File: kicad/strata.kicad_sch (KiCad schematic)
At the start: 80 parts, among them J1 Eurorack Mono Jack, J10 Conn_01x02_Male, J11 Conn_01x04_Male, J12 Conn_01x04_Female, J13 Conn_01x08_Male, J14 Eurorack Mono Jack, J15 Conn_01x08_Female, J16 Eurorack Mono Jack, J17 Eurorack Mono Jack, J18 Eurorack Mono Jack, J19 Eurorack Mono Jack, J2 Eurorack Mono Jack, J20 Eurorack Mono Jack, J24 Eurorack Mono Jack, J25 Eurorack Mono Jack, J26 Eurorack Mono Jack, J27 Eurorack Mono Jack, J28 Eurorack Mono Jack, J29 Eurorack Mono Jack, J3 Eurorack Mono Jack, J30 Eurorack Mono Jack, J31 Eurorack Mono Jack, J32 Conn_01x08_Female, J33 Eurorack Mono Jack, J34 Conn_01x08_Male, J35 Conn_01x08_Female, J36 Conn_01x08_Male, J37 Eurorack Power Small, J38 Conn_02x04_Odd_Even, J4 Eurorack Mono Jack, J49 Eurorack Mono Jack, J5 Conn_01x04_Female, J50 Eurorack Mono Jack, J51 Eurorack Mono Jack, J52 Conn_01x04_Female, J53 Conn_01x04_Male, J6 Conn_01x06_Female, J7 Conn_01x04_Male, J8 Conn_01x06_Male, J9 Conn_01x02_Female, U1 TL072, U2 L78L05_TO92

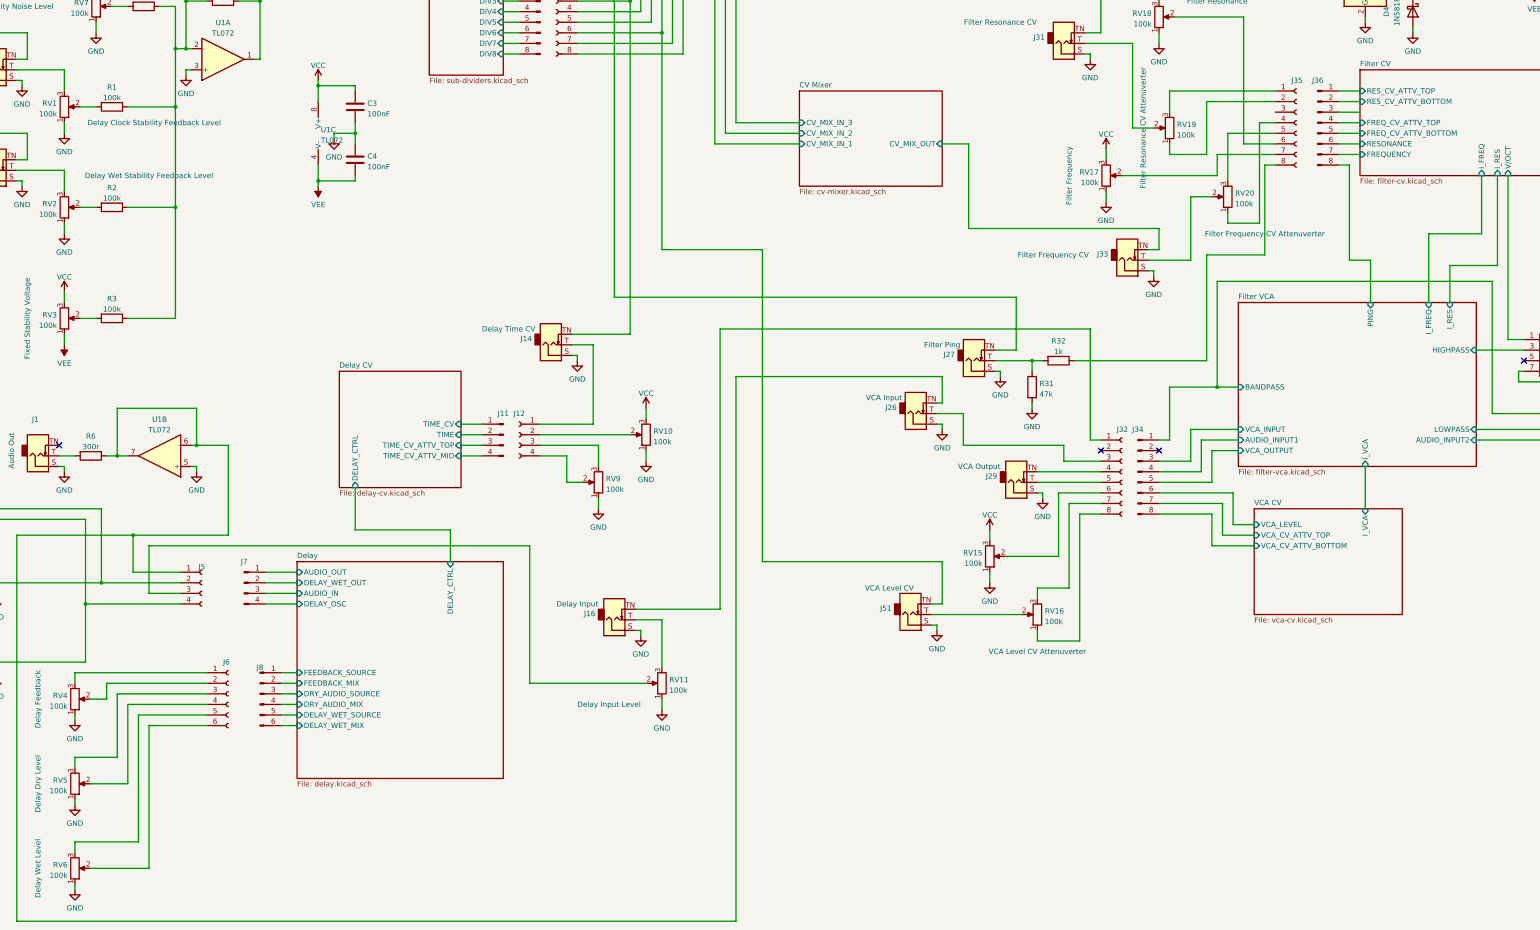
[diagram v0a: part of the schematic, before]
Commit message: component positioning mostly done
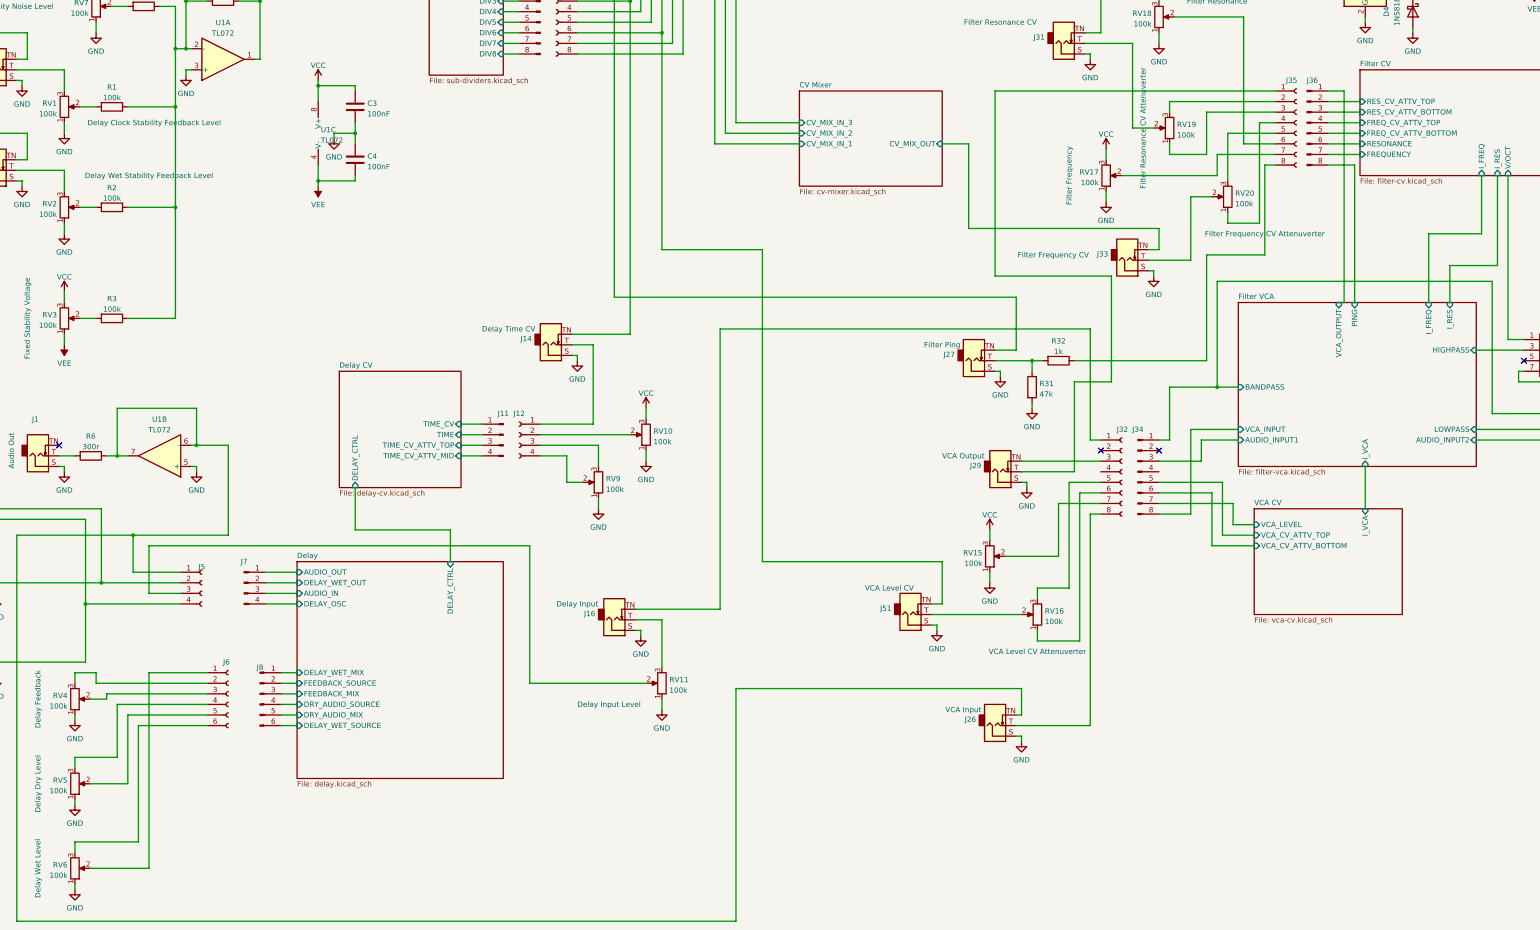
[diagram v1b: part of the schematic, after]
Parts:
- C1, C3, C4: footprint rumblesan-standard-parts:C_Rect_L7.0mm_W3.5mm_P5.00mm -> rumblesan-standard-parts:C_Rect_L7.0mm_W2.5mm_P5.00mm
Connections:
- net Delay/DELAY_WET_MIX: now also J8.1 (Pin_1); no longer J8.6 (Pin_6)
- net Delay/DELAY_WET_SOURCE: now also J8.6 (Pin_6); no longer J8.5 (Pin_5)
- net Delay/DRY_AUDIO_MIX: now also J8.5 (Pin_5); no longer J8.4 (Pin_4)
- net Delay/DRY_AUDIO_SOURCE: now also J8.4 (Pin_4); no longer J8.3 (Pin_3)
- net Delay/FEEDBACK_MIX: now also J8.3 (Pin_3); no longer J8.2 (Pin_2)
- net Delay/FEEDBACK_SOURCE: now also J8.2 (Pin_2); no longer J8.1 (Pin_1)
- net Filter CV/RES_CV_ATTV_BOTTOM: now also J36.3 (Pin_3); no longer J36.2 (Pin_2)
- net Filter CV/RES_CV_ATTV_TOP: now also J36.2 (Pin_2); no longer J36.1 (Pin_1)
- net Filter VCA/AUDIO_INPUT1: now also J34.3 (Pin_3); no longer J34.4 (Pin_4)
- net Filter VCA/VCA_INPUT: now also J34.8 (Pin_8); no longer J34.3 (Pin_3)
- net Filter VCA/VCA_OUTPUT: now also J36.1 (Pin_1); no longer J34.5 (Pin_5)
- net VCA CV/VCA_CV_ATTV_BOTTOM: now also J34.6 (Pin_6); no longer J34.8 (Pin_8)
- net VCA CV/VCA_CV_ATTV_TOP: now also J34.5 (Pin_5); no longer J34.7 (Pin_7)
- net VCA CV/VCA_LEVEL: now also J34.7 (Pin_7); no longer J34.6 (Pin_6)
- net at RV4.2: now also J6.3 (Pin_3); no longer J6.2 (Pin_2)
- net at RV4.3: now also J6.2 (Pin_2); no longer J6.1 (Pin_1)
- net at J35.1 (Pin_1): now also J29.T (Tip); no longer RV19.3
- net at J35.2 (Pin_2): now also RV19.3; no longer RV19.1
- net at J35.3 (Pin_3): now also RV19.1
- net at RV5.2: now also J6.5 (Pin_5); no longer J6.4 (Pin_4)
- net at RV5.3: now also J6.4 (Pin_4); no longer J6.3 (Pin_3)
- net at RV6.3: now also J6.6 (Pin_6); no longer J6.5 (Pin_5)
- net at RV6.2: now also J6.1 (Pin_1); no longer J6.6 (Pin_6)
- net at J32.3 (Pin_3): now also J29.TN (Tip_normalize); no longer J26.T (Tip)
- net at J32.4 (Pin_4): no longer J29.TN (Tip_normalize)
- net at J32.5 (Pin_5): now also RV16.3; no longer J29.T (Tip)
- net at J32.6 (Pin_6): now also RV16.1; no longer RV15.2
- net at J32.7 (Pin_7): now also RV15.2; no longer RV16.3
- net at J32.8 (Pin_8): now also J26.T (Tip); no longer RV16.1
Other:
- moved on the sheet: J26, J29, J36

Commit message: initial layout done
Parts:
- removed H2, H4: MountingHole_Pad, rumblesan-standard-parts:MountingHole_3.2mm_M3_DIN965_Pad, symbol Mechanical:MountingHole_Pad
- removed J32: Conn_01x08_Female, Connector_PinSocket_2.54mm:PinSocket_1x08_P2.54mm_Vertical, symbol Connector:Conn_01x08_Female
- removed J34: Conn_01x08_Male, Connector_PinHeader_2.54mm:PinHeader_1x08_P2.54mm_Vertical, symbol Connector:Conn_01x08_Male
- added J32: Conn_01x06_Female, Connector_PinSocket_2.54mm:PinSocket_1x06_P2.54mm_Vertical, symbol Connector:Conn_01x06_Female
- added J34: Conn_01x06_Male, Connector_PinHeader_2.54mm:PinHeader_1x06_P2.54mm_Vertical, symbol Connector:Conn_01x06_Male
- added R157: 100k, rumblesan-standard-parts:R_Axial_DIN0207_L6.3mm_D2.5mm_P10.16mm_Horizontal, symbol rumblesan-standard-parts:R
- added R65: 47k, rumblesan-standard-parts:R_Axial_DIN0207_L6.3mm_D2.5mm_P10.16mm_Horizontal, symbol rumblesan-standard-parts:R
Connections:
- net CV Mixer/CV_MIX_IN_1: now also J15.4 (Pin_4); no longer J15.3 (Pin_3)
- net Filter CV/FREQ_CV_ATTV_BOTTOM: now also J36.4 (Pin_4); no longer J36.5 (Pin_5)
- net Filter CV/FREQ_CV_ATTV_TOP: now also J36.3 (Pin_3); no longer J36.4 (Pin_4)
- net Filter CV/RES_CV_ATTV_BOTTOM: now also J36.5 (Pin_5); no longer J36.3 (Pin_3)
- net Filter CV/V/OCT: now also J38.3 (Pin_3); no longer J38.1 (Pin_1)
- net Filter VCA/AUDIO_INPUT1: now also J34.5 (Pin_5)
- net Filter VCA/BANDPASS: now also J34.6 (Pin_6)
- net Filter VCA/HIGHPASS: now also J38.1 (Pin_1); no longer J38.3 (Pin_3)
- net Filter VCA/VCA_INPUT: now also J34.2 (Pin_2)
- net GND: now also R157.2, R65.1; no longer U1.5 (+)
- net Sub Dividers/DIV3: now also J13.4 (Pin_4); no longer J13.3 (Pin_3)
- net Sub Dividers/DIV4: now also J13.3 (Pin_3); no longer J13.4 (Pin_4)
- net VCA CV/VCA_CV_ATTV_BOTTOM: now also J34.3 (Pin_3)
- net VCA CV/VCA_CV_ATTV_TOP: now also J34.1 (Pin_1)
- net VCA CV/VCA_LEVEL: now also J34.4 (Pin_4)
- net at C1.2, J9.2 (Pin_2), R5.1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: now also R65.2
- net at R6.1, U1.6 (-), U1.7: no longer J26.TN (Tip_normalize), J5.1 (Pin_1)
- net at J16.TN (Tip_normalize): now also J32.6 (Pin_6)
- net at J35.3 (Pin_3): now also RV20.3; no longer RV19.1
- net at J35.5 (Pin_5): now also RV19.1; no longer RV20.3
- net at J20.T (Tip), J31.TN (Tip_normalize): now also J15.3 (Pin_3); no longer J15.4 (Pin_4)
- net at J29.TN (Tip_normalize): now also J32.5 (Pin_5)
- net at RV16.3: now also J32.1 (Pin_1)
- net at RV16.1: now also J32.3 (Pin_3)
- net at RV15.2: now also J32.4 (Pin_4)
- net at J26.T (Tip): now also J32.2 (Pin_2)
- new net: J26.TN (Tip_normalize), J5.1 (Pin_1), R157.1, U1.5 (+)
- no-connect marks 15 -> 13
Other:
- removed sheet Filter Expander
- moved on the sheet: J1, J26, J27, J29, J51, J6, J8, R31, R32, R6, RV15, RV16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

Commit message: Final changes for rev01
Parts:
- added C72: 22pF, rumblesan-standard-parts:C_Rect_L7.0mm_W2.5mm_P5.00mm, symbol rumblesan-standard-parts:C
- added C73: 1uF, rumblesan-standard-parts:CP_Radial_D5.0mm_P2.00mm, symbol rumblesan-standard-parts:C_Polarized
- added J39: Conn_01x03_Male, Connector_PinHeader_2.54mm:PinHeader_1x03_P2.54mm_Vertical, symbol Connector:Conn_01x03_Male
- added Q17: 2N3904, Package_TO_SOT_THT:TO-92_Inline_Wide, symbol Transistor_BJT:2N3904
- added R158, R159, R160: 10k, rumblesan-standard-parts:R_Axial_DIN0207_L6.3mm_D2.5mm_P10.16mm_Horizontal, symbol rumblesan-standard-parts:R
- added R161: 47k, rumblesan-standard-parts:R_Axial_DIN0207_L6.3mm_D2.5mm_P10.16mm_Horizontal, symbol rumblesan-standard-parts:R
- added R162: 47k, rumblesan-standard-parts:R_Axial_DIN0207_L6.3mm_D2.5mm_P2.54mm_Vertical, symbol rumblesan-standard-parts:R
- added R163, R166, R167, R168, R170, R171: 330r, rumblesan-standard-parts:R_Axial_DIN0207_L6.3mm_D2.5mm_P10.16mm_Horizontal, symbol rumblesan-standard-parts:R
- added R164, R165, R169, R172, R173: 330r, rumblesan-standard-parts:R_Axial_DIN0207_L6.3mm_D2.5mm_P2.54mm_Vertical, symbol rumblesan-standard-parts:R
- R6: value 300r -> 100k
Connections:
- net CV Mixer/CV_MIX_IN_1: now also R167.2; no longer J19.T (Tip)
- net CV Mixer/CV_MIX_IN_2: now also R169.2; no longer J24.T (Tip)
- net CV Mixer/CV_MIX_IN_3: now also R172.2; no longer J28.T (Tip)
- net Delay/DELAY_WET_SOURCE: now also J8.2 (Pin_2); no longer J8.6 (Pin_6)
- net Delay/DRY_AUDIO_MIX: now also J8.3 (Pin_3); no longer J8.5 (Pin_5)
- net Delay/DRY_AUDIO_SOURCE: now also J8.5 (Pin_5); no longer J8.4 (Pin_4)
- net Delay/FEEDBACK_MIX: now also J8.6 (Pin_6); no longer J8.3 (Pin_3)
- net Delay/FEEDBACK_SOURCE: now also J8.4 (Pin_4); no longer J8.2 (Pin_2)
- net GND: now also U1.5 (+), R162.1; no longer R157.2
- net Noise/NOISE: now also R165.1; no longer J4.T (Tip)
- net VCC: now also Q17.3 (C), R158.1; no longer RV3.3
- net VEE: now also R159.2, R160.1; no longer RV3.1
- net at J9.2 (Pin_2), R65.2, U1.1: now also R157.2, C72.2; no longer C1.2, R5.1
- net at C1.1, R1.1, R2.1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: now also U1.6 (-); no longer U1.2 (-)
- net at RV4.2: now also J6.6 (Pin_6); no longer J6.3 (Pin_3)
- net at RV4.3: now also J6.4 (Pin_4); no longer J6.2 (Pin_2)
- net at J3.TN (Tip_normalize), J5.2 (Pin_2): now also R164.2; no longer J49.T (Tip)
- net at J2.TN (Tip_normalize), J5.4 (Pin_4): now also R163.2; no longer J50.T (Tip)
- net at R6.1, U1.7: now also C1.2, R5.1; no longer U1.6 (-)
- net at J15.3 (Pin_3), J31.TN (Tip_normalize): now also R168.2; no longer J20.T (Tip)
- net at J30.T (Tip): now also R173.1; no longer J15.8 (Pin_8)
- net at RV5.2: now also J6.3 (Pin_3); no longer J6.5 (Pin_5)
- net at RV5.3: now also J6.5 (Pin_5); no longer J6.4 (Pin_4)
- net at RV6.3: now also J6.2 (Pin_2); no longer J6.6 (Pin_6)
- net at J15.2 (Pin_2), J27.TN (Tip_normalize): now also R166.2; no longer J18.T (Tip)
- net at J15.6 (Pin_6), J51.TN (Tip_normalize): now also R170.2; no longer J25.T (Tip)
- net at R6.2: now also R157.1, U1.2 (-), C72.1; no longer J1.T (Tip)
- new net: R159.1, RV3.1
- new net: J28.T (Tip), R172.1
- new net: J4.T (Tip), R165.2
- new net: J20.T (Tip), R168.1
- new net: J19.T (Tip), R167.1
- new net: J24.T (Tip), R169.1
- new net: J26.TN (Tip_normalize), R171.1
- new net: J39.3 (Pin_3), J5.1 (Pin_1), R161.1, R171.2
- new net: J49.T (Tip), R164.1
- new net: J50.T (Tip), R163.1
- new net: C73.1, Q17.1 (E), R160.2
- new net: J39.2 (Pin_2), Q17.2 (B), R161.2, R162.2
- new net: R158.2, RV3.3
- new net: J15.8 (Pin_8), R173.2
- new net: J18.T (Tip), R166.1
- new net: C73.2, J1.T (Tip)
- new net: J25.T (Tip), R170.1
- no-connect marks 13 -> 14
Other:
- moved on the sheet: C3, C4, J1, J49, J5, J6, J7, J8, R157, R3, RV3, RV4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
